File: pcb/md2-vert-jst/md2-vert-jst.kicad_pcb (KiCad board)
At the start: 2 copper layers, 18 x 21 mm, 4 parts, among them J1 JST, J2 MD-90SM

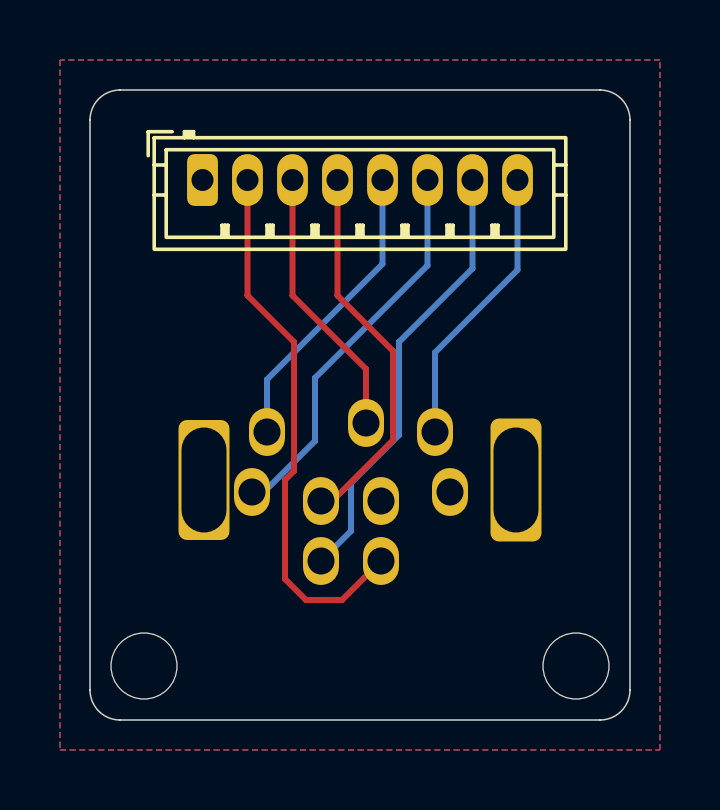
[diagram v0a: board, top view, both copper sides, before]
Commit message: Switcher should run off 5V / RAW pin
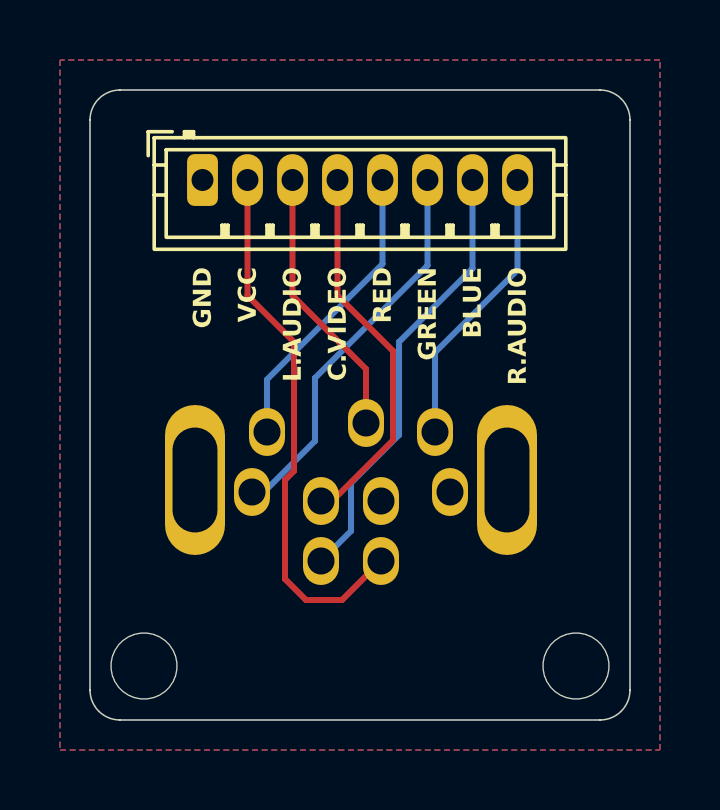
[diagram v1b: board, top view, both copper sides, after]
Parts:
- J2: value MD-90SM -> MDC-9-04; footprint Connector_MiniDIN9_TH_Vertical:MDC-9-04 -> Connector_MiniDIN9_TH_Vertical:MDC-9-04_incorrect_symmetric_shielding
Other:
- board text added: "BLUE"
- board text added: "C.VIDEO"
- board text added: "GND"
- board text added: "GREEN"
- board text added: "L.AUDIO"
- board text added: "R.AUDIO"
- board text added: "RED"
- board text added: "VCC"
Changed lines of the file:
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@@
 		(embedded_fonts no)
 	)
-	(footprint "Connector_MiniDIN9_TH_Vertical:MDC-9-04"
+	(footprint "Connector_MiniDIN9_TH_Vertical:MDC-9-04_incorrect_symmetric_shielding"
 		(layer "B.Cu")
 		(at 99.7 100)
 		(property "Reference" "J2"
-			(at 0 7.545 0)
+			(at 0 7.545 180)
 			(layer "B.SilkS")
 			(hide yes)
@@
 			)
 		)
-		(property "Value" "MD-90SM"
-			(at 0 -7.545 0)
-			(layer "B.Fab")
+		(property "Value" "MDC-9-04"
+			(at 0 -4.2 180)
+			(layer "B.SilkS")
 			(effects
 				(font
@@
 		)
 		(property "Datasheet" ""
+			(at 0 0 180)
+			(layer "B.Fab")
+			(hide yes)
+			(effects
+				(font
+					(size 1.27 1.27)
+					(thickness 0.15)
+				)
+				(justify mirror)
+			)
+		)
+		(property "Description" ""
+			(at 0 0 180)
+			(layer "B.Fab")
+			(hide yes)
+			(effects
+				(font
+					(size 1.27 1.27)
+					(thickness 0.15)
+				)
+				(justify mirror)
+			)
+		)
+		(property "STANDARD" "Manufacturer Recommendations"
 			(at 0 0 0)
-			(layer "B.Fab")
-			(hide yes)
-			(effects
-				(font
-					(size 1.27 1.27)
-					(thickness 0.15)
-				)
-				(justify mirror)
-			)
-		)
-		(property "Description" ""
+			(unlocked yes)
+			(layer "B.Fab")
+			(hide yes)
+			(effects
+				(font
+					(size 1 1)
+					(thickness 0.15)
+				)
+				(justify mirror)
+			)
+		)
+		(property "MAXIMUM_PACKAGE_HEIGHT" "13.6 mm"
 			(at 0 0 0)
-			(layer "B.Fab")
-			(hide yes)
-			(effects
-				(font
-					(size 1.27 1.27)
-					(thickness 0.15)
-				)
-				(justify mirror)
-			)
-		)
-		(property "STANDARD" "Manufacturer Recommendations"
-			(at 0 0 180)
 			(unlocked yes)
 			(layer "B.Fab")
@@
 			)
 		)
-		(property "MAXIMUM_PACKAGE_HEIGHT" "13.6 mm"
-			(at 0 0 180)
+		(property "MANUFACTURER" "CUI"
+			(at 0 0 0)
 			(unlocked yes)
 			(layer "B.Fab")
@@
 			)
 		)
-		(property "MANUFACTURER" "CUI"
-			(at 0 0 180)
-			(unlocked yes)
-			(layer "B.Fab")
-			(hide yes)
-			(effects
-				(font
-					(size 1 1)
-					(thickness 0.15)
-				)
-				(justify mirror)
-			)
-		)
 		(property "PARTREV" "02/18/2022"
-			(at 0 0 180)
+			(at 0 0 0)
 			(unlocked yes)
 			(layer "B.Fab")
@@
 		(sheetfile "md2-vert-jst.kicad_sch")
 		(fp_circle
-			(center 0.3 0)
-			(end 0.3 -6.62)
+			(center 0 0)
+			(end 0 -6.62)
 			(stroke
 				(width 0.12)
@@
 		)
 		(fp_circle
-			(center 0.3 0)
-			(end 0.3 -6.87)
+			(center 0 0)
+			(end 0 -6.87)
 			(stroke
 				(width 0.05)
@@
 		)
 		(fp_circle
-			(center 0.3 0)
-			(end 0.3 -6.5)
+			(center 0 0)
+			(end 0 -6.5)
 			(stroke
 				(width 0.1)
@@
 		)
 		(fp_text user "${REFERENCE}"
-			(at 0 -9 0)
+			(at 0 -9 180)
 			(layer "B.Fab")
 			(effects
@@
 			(thermal_bridge_angle 45)
 		)
-		(pad "S1" thru_hole roundrect
-			(at -4.9 0)
-			(size 1.7 4)
+		(pad "S1" thru_hole oval
+			(at -5.2 0)
+			(size 2 5)
 			(drill oval 1.5 3.5)
 			(layers "*.Cu" "*.Mask")
 			(remove_unused_layers no)
-			(roundrect_rratio 0.1666666667)
 			(net 3 "/GND")
 			(pinfunction "SHIELD")
@@
 			(thermal_bridge_angle 45)
 		)
-		(pad "S2" thru_hole roundrect
-			(at 5.5 0)
-			(size 1.7 4.1)
+		(pad "S2" thru_hole oval
+			(at 5.2 0)
+			(size 2 5)
 			(drill oval 1.5 3.5)
 			(layers "*.Cu" "*.Mask")
 			(remove_unused_layers no)
-			(roundrect_rratio 0.1666666667)
 			(net 3 "/GND")
 			(pinfunction "SHIELD")
@@
 		(layer "Edge.Cuts")
 	)
+	(gr_text "VCC"
+		(at 96.6 92.9 90)
+		(layer "F.SilkS")
+		(effects
+			(font
+				(size 0.6 0.6)
+				(thickness 0.1)
+				(bold yes)
+			)
+			(justify right bottom)
+		)
+	)
+	(gr_text "BLUE"
+		(at 104.1 92.9 90)
+		(layer "F.SilkS")
+		(effects
+			(font
+				(size 0.6 0.6)
+				(thickness 0.1)
+				(bold yes)
+			)
+			(justify right bottom)
+		)
+	)
+	(gr_text "GREEN"
+		(at 102.6 92.9 90)
+		(layer "F.SilkS")
+		(effects
+			(font
+				(size 0.6 0.6)
+				(thickness 0.1)
+				(bold yes)
+			)
+			(justify right bottom)
+		)
+	)
+	(gr_text "C.VIDEO"
+		(at 99.6 92.9 90)
+		(layer "F.SilkS")
+		(effects
+			(font
+				(size 0.6 0.6)
+				(thickness 0.1)
+				(bold yes)
+			)
+			(justify right bottom)
+		)
+	)
+	(gr_text "L.AUDIO"
+		(at 98.1 92.9 90)
+		(layer "F.SilkS")
+		(effects
+			(font
+				(size 0.6 0.6)
+				(thickness 0.1)
+				(bold yes)
+			)
+			(justify right bottom)
+		)
+	)
+	(gr_text "GND"
+		(at 95.1 92.9 90)
+		(layer "F.SilkS")
+		(effects
+			(font
+				(size 0.6 0.6)
+				(thickness 0.1)
+				(bold yes)
+			)
+			(justify right bottom)
+		)
+	)
+	(gr_text "R.AUDIO"
+		(at 105.6 92.9 90)
+		(layer "F.SilkS")
+		(effects
+			(font
+				(size 0.6 0.6)
+				(thickness 0.1)
+				(bold yes)
+			)
+			(justify right bottom)
+		)
+	)
+	(gr_text "RED"
+		(at 101.1 92.9 90)
+		(layer "F.SilkS")
+		(effects
+			(font
+				(size 0.6 0.6)
+				(thickness 0.1)
+				(bold yes)
+			)
+			(justify right bottom)
+		)
+	)
 	(segment
